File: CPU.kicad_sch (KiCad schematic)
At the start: 215 parts, among them J1 Conn_02x36_Top_Bottom, P10 Conn_02x08_Counter_Clockwise, P2 Conn_02x13_Top_Bottom, P3 Conn_02x13_Top_Bottom, P4 Conn_02x08_Counter_Clockwise, P5 Conn_02x25_Counter_Clockwise, P6 Conn_02x25_Counter_Clockwise, P7 Conn_02x07_Counter_Clockwise, P8 Conn_02x08_Counter_Clockwise

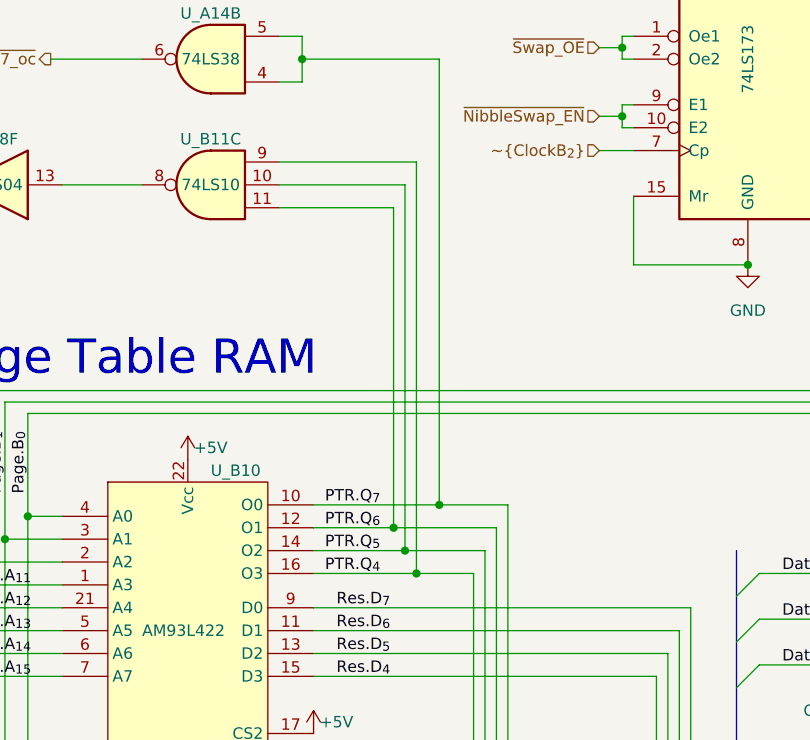
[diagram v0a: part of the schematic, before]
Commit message: Swap U_B11C inputs
Lays out much better
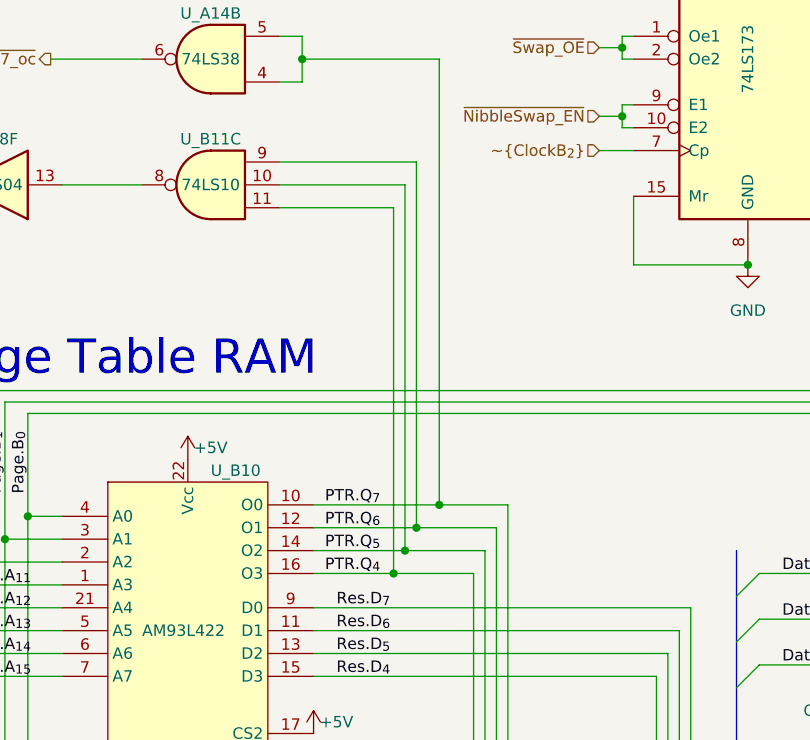
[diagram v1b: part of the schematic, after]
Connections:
- net PTR.Q_{4}: now also U_B11.11; no longer U_B11.9
- net PTR.Q_{6}: now also U_B11.9; no longer U_B11.11
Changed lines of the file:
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@@
   (junction (at 604.52 29.21) (diameter 0) (color 0 0 0 0)
   )
-  (junction (at 238.76 288.29) (diameter 0) (color 0 0 0 0)
-  )
   (junction (at 775.97 29.21) (diameter 0) (color 0 0 0 0)
   )
@@
   (junction (at 862.33 769.62) (diameter 0) (color 0 0 0 0)
   )
-  (junction (at 241.3 293.37) (diameter 0) (color 0 0 0 0)
-  )
   (junction (at 610.87 760.73) (diameter 0) (color 0 0 0 0)
   )
@@
   (junction (at 1009.65 680.72) (diameter 0) (color 0 0 0 0)
   )
+  (junction (at 241.3 288.29) (diameter 0) (color 0 0 0 0)
+  )
   (junction (at 499.11 241.3) (diameter 0) (color 0 0 0 0)
   )
@@
   (junction (at 449.58 327.66) (diameter 0) (color 0 0 0 0)
   )
+  (junction (at 238.76 293.37) (diameter 0) (color 0 0 0 0)
+  )
   (junction (at 793.75 756.92) (diameter 0) (color 0 0 0 0)
   )
@@
     (stroke (width 0) (type default) (color 0 0 0 0))
   )
-  (wire (pts (xy 229.87 288.29) (xy 238.76 288.29))
-    (stroke (width 0) (type default) (color 0 0 0 0))
-  )
   (wire (pts (xy 407.67 119.38) (xy 415.29 119.38))
     (stroke (width 0) (type default) (color 0 0 0 0))
@@
     (stroke (width 0) (type default) (color 0 0 0 0))
   )
-  (wire (pts (xy 229.87 293.37) (xy 241.3 293.37))
-    (stroke (width 0) (type default) (color 0 0 0 0))
-  )
   (wire (pts (xy 638.81 29.21) (xy 650.24 29.21))
     (stroke (width 0) (type default) (color 0 0 0 0))
@@
     (stroke (width 0) (type default) (color 0 0 0 0))
   )
+  (wire (pts (xy 238.76 293.37) (xy 247.65 293.37))
+    (stroke (width 0) (type default) (color 0 0 0 0))
+  )
   (wire (pts (xy 455.93 396.24) (xy 466.09 396.24))
     (stroke (width 0) (type default) (color 0 0 0 0))
@@
     (stroke (width 0) (type default) (color 0 0 0 0))
   )
-  (wire (pts (xy 238.76 252.73) (xy 238.76 288.29))
-    (stroke (width 0) (type default) (color 0 0 0 0))
-  )
   (wire (pts (xy 855.98 54.61) (xy 867.41 54.61))
     (stroke (width 0) (type default) (color 0 0 0 0))
@@
     (stroke (width 0) (type default) (color 0 0 0 0))
   )
-  (wire (pts (xy 250.19 288.29) (xy 238.76 288.29))
+  (wire (pts (xy 250.19 288.29) (xy 241.3 288.29))
     (stroke (width 0) (type default) (color 0 0 0 0))
   )
@@
     (stroke (width 0) (type default) (color 189 121 184 1))
   )
-  (wire (pts (xy 241.3 247.65) (xy 241.3 293.37))
+  (wire (pts (xy 241.3 247.65) (xy 241.3 288.29))
     (stroke (width 0) (type default) (color 0 0 0 0))
   )
@@
     (stroke (width 0) (type default) (color 0 0 0 0))
   )
+  (wire (pts (xy 229.87 288.29) (xy 241.3 288.29))
+    (stroke (width 0) (type default) (color 0 0 0 0))
+  )
   (wire (pts (xy 915.67 252.73) (xy 896.62 252.73))
     (stroke (width 0) (type default) (color 0 0 0 0))
@@
     (stroke (width 0) (type default) (color 0 0 0 0))
   )
+  (wire (pts (xy 238.76 252.73) (xy 238.76 293.37))
+    (stroke (width 0) (type default) (color 0 0 0 0))
+  )
   (wire (pts (xy 991.87 523.24) (xy 958.85 523.24))
     (stroke (width 0) (type default) (color 0 0 0 0))
@@
     (stroke (width 0) (type default) (color 0 0 0 0))
   )
-  (wire (pts (xy 241.3 293.37) (xy 247.65 293.37))
+  (wire (pts (xy 229.87 293.37) (xy 238.76 293.37))
     (stroke (width 0) (type default) (color 0 0 0 0))
   )

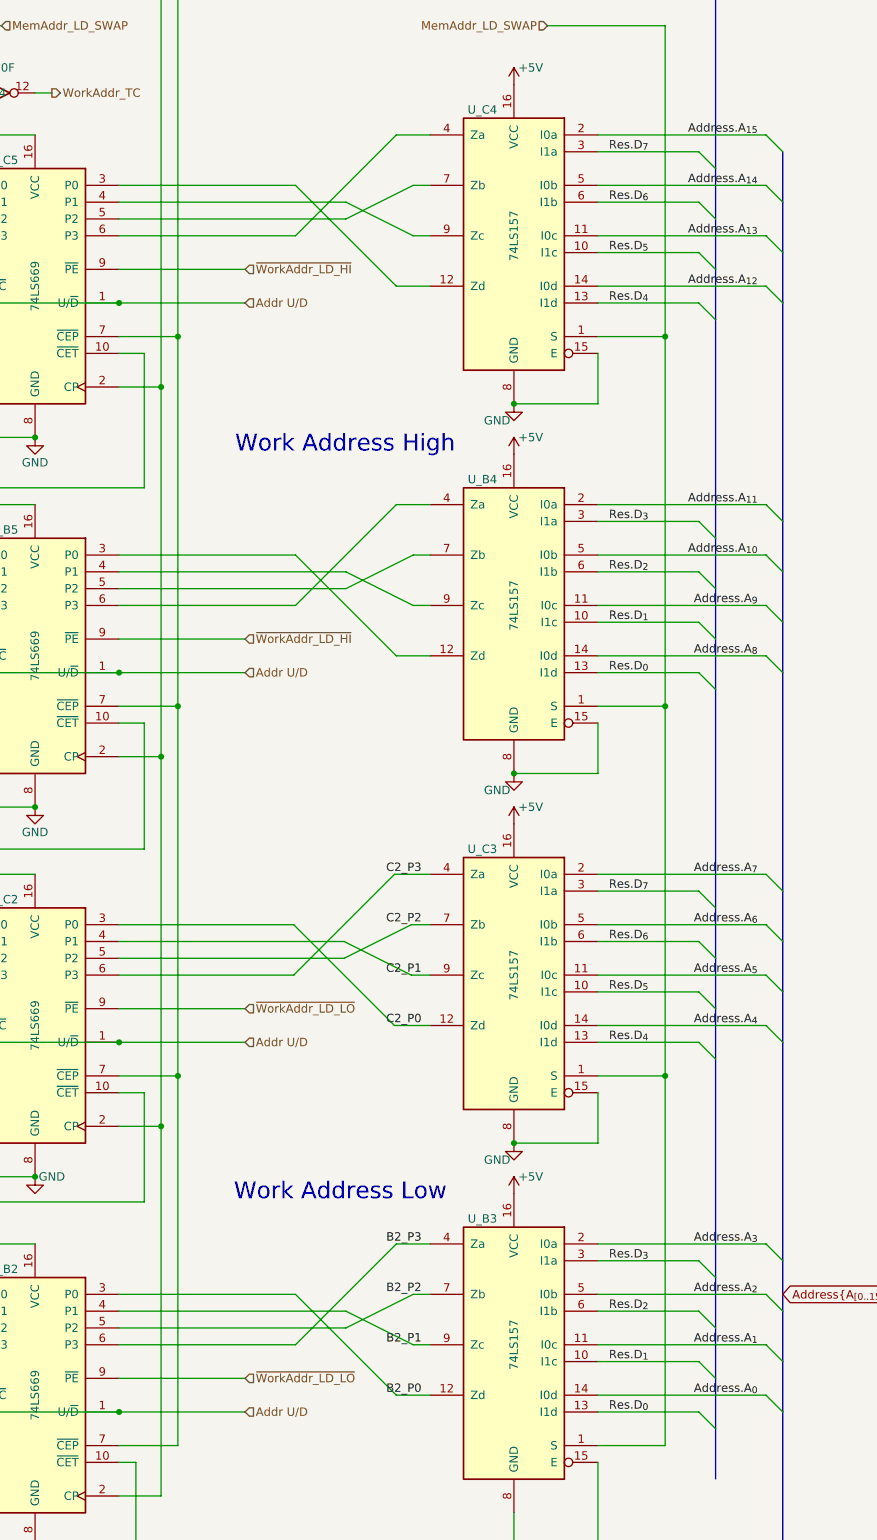
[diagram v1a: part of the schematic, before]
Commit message: Rearrange work address mux pins
B3, B4, C3, C4 now route much better
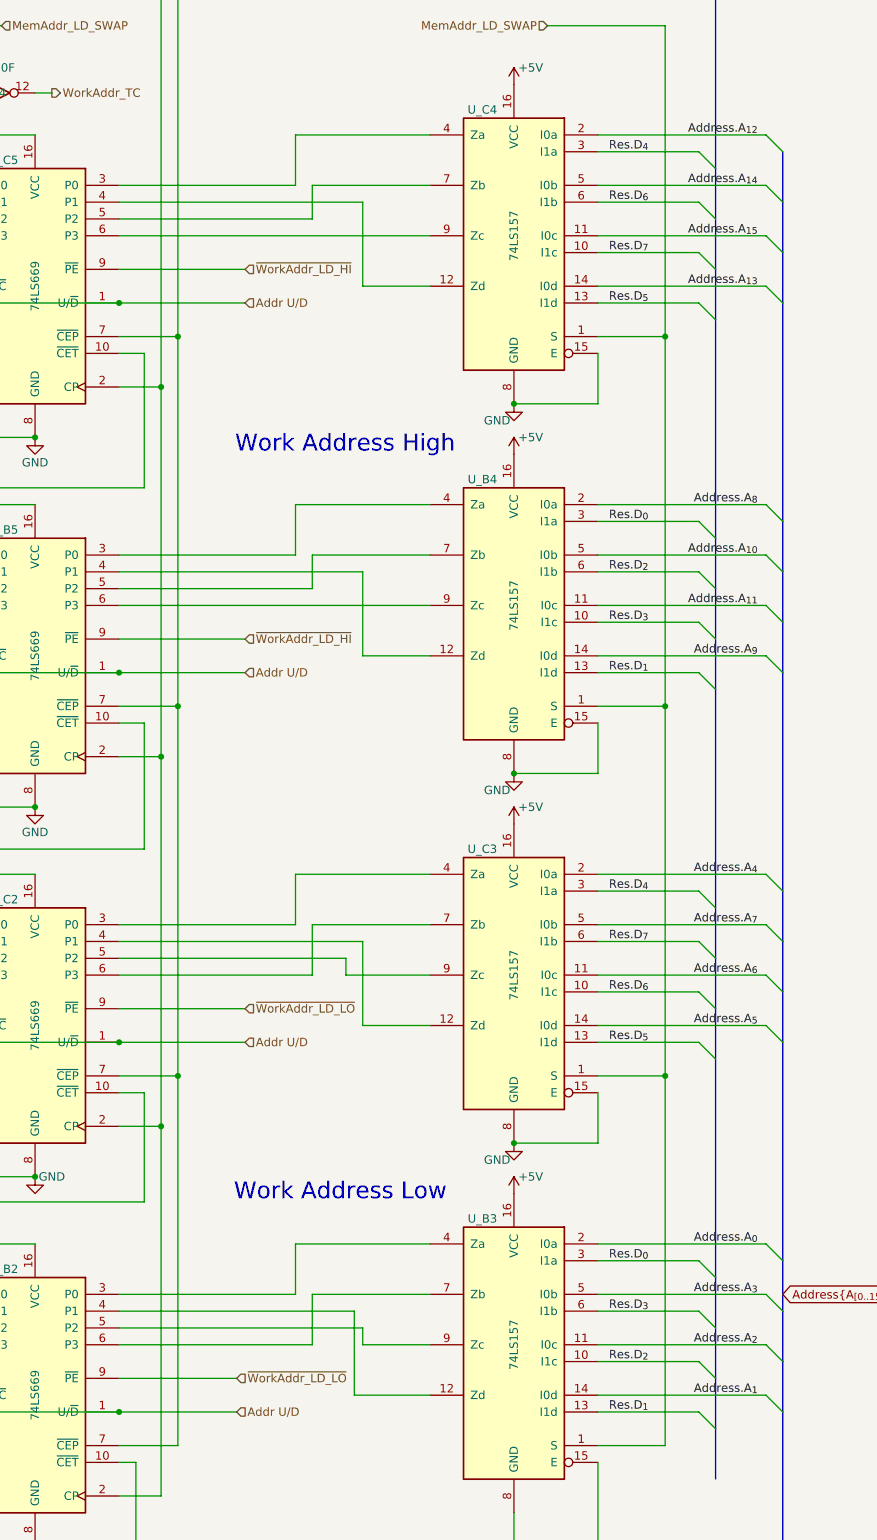
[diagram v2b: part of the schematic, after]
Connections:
- net Address.A_{0}: now also U_B3.2 (I0a); no longer U_B3.14 (I0d)
- net Address.A_{11}: now also U_B4.11 (I0c); no longer U_B4.2 (I0a)
- net Address.A_{12}: now also U_C4.2 (I0a); no longer U_C4.14 (I0d)
- net Address.A_{13}: now also U_C4.14 (I0d); no longer U_C4.11 (I0c)
- net Address.A_{15}: now also U_C4.11 (I0c); no longer U_C4.2 (I0a)
- net Address.A_{1}: now also U_B3.14 (I0d); no longer U_B3.11 (I0c)
- net Address.A_{2}: now also U_B3.11 (I0c); no longer U_B3.5 (I0b)
- net Address.A_{3}: now also U_B3.5 (I0b); no longer U_B3.2 (I0a)
- net Address.A_{4}: now also U_C3.2 (I0a); no longer U_C3.14 (I0d)
- net Address.A_{5}: now also U_C3.14 (I0d); no longer U_C3.11 (I0c)
- net Address.A_{6}: now also U_C3.11 (I0c); no longer U_C3.5 (I0b)
- net Address.A_{7}: now also U_C3.5 (I0b); no longer U_C3.2 (I0a)
- net Address.A_{8}: now also U_B4.2 (I0a); no longer U_B4.14 (I0d)
- net Address.A_{9}: now also U_B4.14 (I0d); no longer U_B4.11 (I0c)
- net Res.D_{0}: now also U_B3.3 (I1a), U_B4.3 (I1a); no longer U_B3.13 (I1d), U_B4.13 (I1d)
- net Res.D_{1}: now also U_B3.13 (I1d), U_B4.13 (I1d); no longer U_B3.10 (I1c), U_B4.10 (I1c)
- net Res.D_{2}: now also U_B3.10 (I1c); no longer U_B3.6 (I1b)
- net Res.D_{3}: now also U_B3.6 (I1b), U_B4.10 (I1c); no longer U_B3.3 (I1a), U_B4.3 (I1a)
- net Res.D_{4}: now also U_C3.3 (I1a), U_C4.3 (I1a); no longer U_C3.13 (I1d), U_C4.13 (I1d)
- net Res.D_{5}: now also U_C3.13 (I1d), U_C4.13 (I1d); no longer U_C3.10 (I1c), U_C4.10 (I1c)
- net Res.D_{6}: now also U_C3.10 (I1c); no longer U_C3.6 (I1b)
- net Res.D_{7}: now also U_C3.6 (I1b), U_C4.10 (I1c); no longer U_C3.3 (I1a), U_C4.3 (I1a)
- net at U_C5.3 (P0): now also U_C4.4 (Za); no longer U_C4.12 (Zd)
- net at U_C5.4 (P1): now also U_C4.12 (Zd); no longer U_C4.9 (Zc)
- net at U_C5.6 (P3): now also U_C4.9 (Zc); no longer U_C4.4 (Za)
- net at U_B4.12 (Zd): now also U_B5.4 (P1); no longer U_B5.3 (P0)
- net at U_B4.4 (Za): now also U_B5.3 (P0); no longer U_B5.6 (P3)
- net at U_B4.9 (Zc): now also U_B5.6 (P3); no longer U_B5.4 (P1)
- net B2_P0: no longer names the net of U_B3.12 (Zd)
- net B2_P0: now also U_B2.4 (P1); no longer U_B2.3 (P0)
- net B2_P1: no longer names the net of U_B3.9 (Zc)
- net B2_P1: now also U_B2.5 (P2); no longer U_B2.4 (P1)
- net B2_P2: no longer names the net of U_B3.7 (Zb)
- net B2_P2: now also U_B2.6 (P3); no longer U_B2.5 (P2)
- net B2_P3: no longer names the net of U_B3.4 (Za)
- net B2_P3: now also U_B2.3 (P0); no longer U_B2.6 (P3)
- net C2_P0: no longer names the net of U_C3.12 (Zd)
- net C2_P0: now also U_C2.4 (P1); no longer U_C2.3 (P0)
- net C2_P1: no longer names the net of U_C3.9 (Zc)
- net C2_P1: now also U_C2.5 (P2); no longer U_C2.4 (P1)
- net C2_P2: no longer names the net of U_C3.7 (Zb)
- net C2_P2: now also U_C2.6 (P3); no longer U_C2.5 (P2)
- net C2_P3: no longer names the net of U_C3.4 (Za)
- net C2_P3: now also U_C2.3 (P0); no longer U_C2.6 (P3)
